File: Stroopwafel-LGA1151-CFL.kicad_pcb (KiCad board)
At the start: 2 copper layers, 4 parts

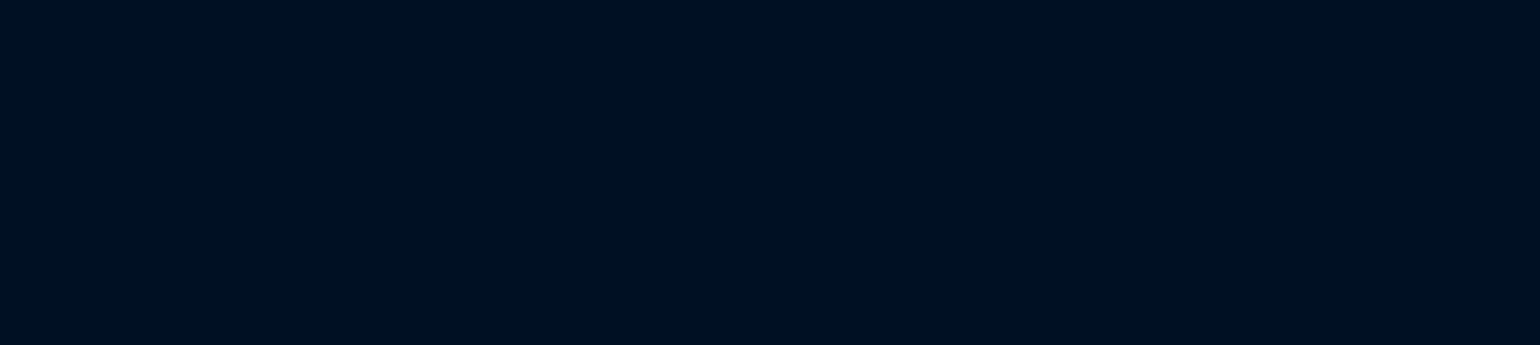
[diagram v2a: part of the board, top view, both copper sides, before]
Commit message: Added PCIe x16 slot
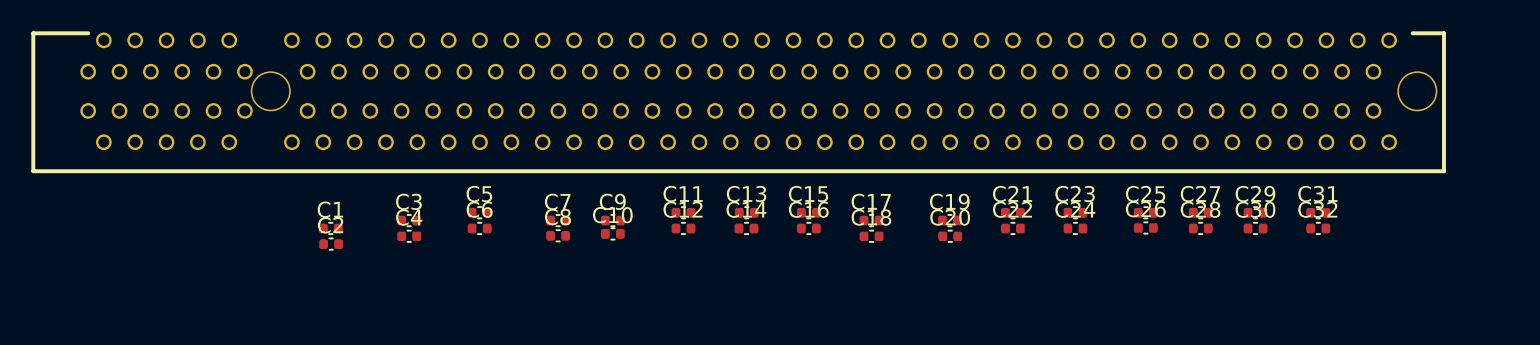
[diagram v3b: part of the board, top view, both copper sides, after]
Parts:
- added C1: 0.22uF, Capacitor_SMD:C_0402_1005Metric, F.Cu at (139.0, 38.0)
- added C10: 0.22uF, Capacitor_SMD:C_0402_1005Metric, F.Cu at (157.0, 38.4)
- added C11: 0.22uF, Capacitor_SMD:C_0402_1005Metric, F.Cu at (161.5, 37.0)
- added C12: 0.22uF, Capacitor_SMD:C_0402_1005Metric, F.Cu at (161.5, 38.0)
- added C13: 0.22uF, Capacitor_SMD:C_0402_1005Metric, F.Cu at (165.5, 37.0)
- added C14: 0.22uF, Capacitor_SMD:C_0402_1005Metric, F.Cu at (165.5, 38.0)
- added C15: 0.22uF, Capacitor_SMD:C_0402_1005Metric, F.Cu at (169.5, 37.0)
- added C16: 0.22uF, Capacitor_SMD:C_0402_1005Metric, F.Cu at (169.5, 38.0)
- added C17: 0.22uF, Capacitor_SMD:C_0402_1005Metric, F.Cu at (173.5, 37.5)
- added C18: 0.22uF, Capacitor_SMD:C_0402_1005Metric, F.Cu at (173.5, 38.5)
- added C19: 0.22uF, Capacitor_SMD:C_0402_1005Metric, F.Cu at (178.5, 37.5)
- added C2: 0.22uF, Capacitor_SMD:C_0402_1005Metric, F.Cu at (139.0, 39.0)
- added C20: 0.22uF, Capacitor_SMD:C_0402_1005Metric, F.Cu at (178.5, 38.5)
- added C21: 0.22uF, Capacitor_SMD:C_0402_1005Metric, F.Cu at (182.5, 37.0)
- added C22: 0.22uF, Capacitor_SMD:C_0402_1005Metric, F.Cu at (182.5, 38.0)
- added C23: 0.22uF, Capacitor_SMD:C_0402_1005Metric, F.Cu at (186.5, 37.0)
- added C24: 0.22uF, Capacitor_SMD:C_0402_1005Metric, F.Cu at (186.5, 38.0)
- added C25: 0.22uF, Capacitor_SMD:C_0402_1005Metric, F.Cu at (191.0, 37.0)
- added C26: 0.22uF, Capacitor_SMD:C_0402_1005Metric, F.Cu at (191.0, 38.0)
- added C27: 0.22uF, Capacitor_SMD:C_0402_1005Metric, F.Cu at (194.5, 37.0)
- added C28: 0.22uF, Capacitor_SMD:C_0402_1005Metric, F.Cu at (194.5, 38.0)
- added C29: 0.22uF, Capacitor_SMD:C_0402_1005Metric, F.Cu at (198.0, 37.0)
- added C3: 0.22uF, Capacitor_SMD:C_0402_1005Metric, F.Cu at (144.0, 37.5)
- added C30: 0.22uF, Capacitor_SMD:C_0402_1005Metric, F.Cu at (198.0, 38.0)
- added C31: 0.22uF, Capacitor_SMD:C_0402_1005Metric, F.Cu at (202.0, 37.0)
- added C32: 0.22uF, Capacitor_SMD:C_0402_1005Metric, F.Cu at (202.0, 38.0)
- added C4: 0.22uF, Capacitor_SMD:C_0402_1005Metric, F.Cu at (144.0, 38.5)
- added C5: 0.22uF, Capacitor_SMD:C_0402_1005Metric, F.Cu at (148.5, 37.0)
- added C6: 0.22uF, Capacitor_SMD:C_0402_1005Metric, F.Cu at (148.5, 38.0)
- added C7: 0.22uF, Capacitor_SMD:C_0402_1005Metric, F.Cu at (153.5, 37.5)
- added C8: 0.22uF, Capacitor_SMD:C_0402_1005Metric, F.Cu at (153.5, 38.5)
- added C9: 0.22uF, Capacitor_SMD:C_0402_1005Metric, F.Cu at (157.0, 37.5)
- added J1: PCIe_x16_full, A-my-stuff:PCIe_x16_tht_smallholes, F.Cu at (165.0, 29.2)
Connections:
- JCPU1 pad A5: unconnected-(JCPU1C-PEG_TXP_0-PadA5) -> PCIe_CPU_Tx0+
- JCPU1 pad A6: unconnected-(JCPU1C-PEG_TXN_0-PadA6) -> PCIe_CPU_Tx0-
- JCPU1 pad B4: unconnected-(JCPU1C-PEG_TXP_1-PadB4) -> PCIe_CPU_Tx1+
- JCPU1 pad B5: unconnected-(JCPU1C-PEG_TXN_1-PadB5) -> PCIe_CPU_Tx1-
- JCPU1 pad B7: unconnected-(JCPU1C-PEG_RXN_0-PadB7) -> PCIe_CPU_Rx0-
- JCPU1 pad B8: unconnected-(JCPU1C-PEG_RXP_0-PadB8) -> PCIe_CPU_Rx0+
- JCPU1 pad C3: unconnected-(JCPU1C-PEG_TXP_2-PadC3) -> PCIe_CPU_Tx2+
- JCPU1 pad C4: unconnected-(JCPU1C-PEG_TXN_2-PadC4) -> PCIe_CPU_Tx2-
- JCPU1 pad C6: unconnected-(JCPU1C-PEG_RXN_1-PadC6) -> PCIe_CPU_Rx1-
- JCPU1 pad C7: unconnected-(JCPU1C-PEG_RXP_1-PadC7) -> PCIe_CPU_Rx1+
- JCPU1 pad D2: unconnected-(JCPU1C-PEG_TXP_3-PadD2) -> PCIe_CPU_Tx3+
- JCPU1 pad D3: unconnected-(JCPU1C-PEG_TXN_3-PadD3) -> PCIe_CPU_Tx3-
- JCPU1 pad D5: unconnected-(JCPU1C-PEG_RXN_2-PadD5) -> PCIe_CPU_Rx2-
- JCPU1 pad D6: unconnected-(JCPU1C-PEG_RXP_2-PadD6) -> PCIe_CPU_Rx2+
- JCPU1 pad E1: unconnected-(JCPU1C-PEG_TXP_4-PadE1) -> PCIe_CPU_Tx4+
- JCPU1 pad E2: unconnected-(JCPU1C-PEG_TXN_4-PadE2) -> PCIe_CPU_Tx4-
- JCPU1 pad E4: unconnected-(JCPU1C-PEG_RXN_3-PadE4) -> PCIe_CPU_Rx3-
- JCPU1 pad E5: unconnected-(JCPU1C-PEG_RXP_3-PadE5) -> PCIe_CPU_Rx3+
- JCPU1 pad F2: unconnected-(JCPU1C-PEG_TXP_5-PadF2) -> PCIe_CPU_Tx5+
- JCPU1 pad F3: unconnected-(JCPU1C-PEG_TXN_5-PadF3) -> PCIe_CPU_Tx5-
- JCPU1 pad F5: unconnected-(JCPU1C-PEG_RXN_4-PadF5) -> PCIe_CPU_Rx4-
- JCPU1 pad F6: unconnected-(JCPU1C-PEG_RXP_4-PadF6) -> PCIe_CPU_Rx4+
- JCPU1 pad G1: unconnected-(JCPU1C-PEG_TXP_6-PadG1) -> PCIe_CPU_Tx6+
- JCPU1 pad G2: unconnected-(JCPU1C-PEG_TXN_6-PadG2) -> PCIe_CPU_Tx6-
- JCPU1 pad G4: unconnected-(JCPU1C-PEG_RXN_5-PadG4) -> PCIe_CPU_Rx5-
- JCPU1 pad G5: unconnected-(JCPU1C-PEG_RXP_5-PadG5) -> PCIe_CPU_Rx5+
- JCPU1 pad H2: unconnected-(JCPU1C-PEG_TXP_7-PadH2) -> PCIe_CPU_Tx7+
- JCPU1 pad H3: unconnected-(JCPU1C-PEG_TXN_7-PadH3) -> PCIe_CPU_Tx7-
- JCPU1 pad H5: unconnected-(JCPU1C-PEG_RXN_6-PadH5) -> PCIe_CPU_Rx6-
- JCPU1 pad H6: unconnected-(JCPU1C-PEG_RXP_6-PadH6) -> PCIe_CPU_Rx6+
- JCPU1 pad J1: unconnected-(JCPU1C-PEG_TXP_8-PadJ1) -> PCIe_CPU_Tx8+
- JCPU1 pad J2: unconnected-(JCPU1C-PEG_TXN_8-PadJ2) -> PCIe_CPU_Tx8-
- JCPU1 pad J4: unconnected-(JCPU1C-PEG_RXN_7-PadJ4) -> PCIe_CPU_Rx7-
- JCPU1 pad J5: unconnected-(JCPU1C-PEG_RXP_7-PadJ5) -> PCIe_CPU_Rx7+
- JCPU1 pad K2: unconnected-(JCPU1C-PEG_TXP_9-PadK2) -> PCIe_CPU_Tx9+
- JCPU1 pad K3: unconnected-(JCPU1C-PEG_TXN_9-PadK3) -> PCIe_CPU_Tx9-
- JCPU1 pad K5: unconnected-(JCPU1C-PEG_RXN_8-PadK5) -> PCIe_CPU_Rx8-
- JCPU1 pad K6: unconnected-(JCPU1C-PEG_RXP_8-PadK6) -> PCIe_CPU_Rx8+
- JCPU1 pad L1: unconnected-(JCPU1C-PEG_TXP_10-PadL1) -> PCIe_CPU_Tx10+
- JCPU1 pad L2: unconnected-(JCPU1C-PEG_TXN_10-PadL2) -> PCIe_CPU_Tx10-
- JCPU1 pad L4: unconnected-(JCPU1C-PEG_RXN_9-PadL4) -> PCIe_CPU_Rx9-
- JCPU1 pad L5: unconnected-(JCPU1C-PEG_RXP_9-PadL5) -> PCIe_CPU_Rx9+
- JCPU1 pad M2: unconnected-(JCPU1C-PEG_TXP_11-PadM2) -> PCIe_CPU_Tx11+
- JCPU1 pad M3: unconnected-(JCPU1C-PEG_TXN_11-PadM3) -> PCIe_CPU_Tx11-
- JCPU1 pad M5: unconnected-(JCPU1C-PEG_RXN_10-PadM5) -> PCIe_CPU_Rx10-
- JCPU1 pad M6: unconnected-(JCPU1C-PEG_RXP_10-PadM6) -> PCIe_CPU_Rx10+
- JCPU1 pad N1: unconnected-(JCPU1C-PEG_TXP_12-PadN1) -> PCIe_CPU_Tx12+
- JCPU1 pad N2: unconnected-(JCPU1C-PEG_TXN_12-PadN2) -> PCIe_CPU_Tx12-
- JCPU1 pad N4: unconnected-(JCPU1C-PEG_RXN_11-PadN4) -> PCIe_CPU_Rx11-
- JCPU1 pad N5: unconnected-(JCPU1C-PEG_RXP_11-PadN5) -> PCIe_CPU_Rx11+
- JCPU1 pad P2: unconnected-(JCPU1C-PEG_TXP_13-PadP2) -> PCIe_CPU_Tx13+
- JCPU1 pad P3: unconnected-(JCPU1C-PEG_TXN_13-PadP3) -> PCIe_CPU_Tx13-
- JCPU1 pad P5: unconnected-(JCPU1C-PEG_RXN_12-PadP5) -> PCIe_CPU_Rx12-
- JCPU1 pad P6: unconnected-(JCPU1C-PEG_RXP_12-PadP6) -> PCIe_CPU_Rx12+
- JCPU1 pad R1: unconnected-(JCPU1C-PEG_TXN_14-PadR1) -> PCIe_CPU_Tx14-
- JCPU1 pad R2: unconnected-(JCPU1C-PEG_TXP_14-PadR2) -> PCIe_CPU_Tx14+
- JCPU1 pad R4: unconnected-(JCPU1C-PEG_RXN_13-PadR4) -> PCIe_CPU_Rx13-
- JCPU1 pad R5: unconnected-(JCPU1C-PEG_RXP_13-PadR5) -> PCIe_CPU_Rx13+
- JCPU1 pad T2: unconnected-(JCPU1C-PEG_TXP_15-PadT2) -> PCIe_CPU_Tx15+
- JCPU1 pad T3: unconnected-(JCPU1C-PEG_TXN_15-PadT3) -> PCIe_CPU_Tx15-
- JCPU1 pad T5: unconnected-(JCPU1C-PEG_RXN_14-PadT5) -> PCIe_CPU_Rx14-
- JCPU1 pad T6: unconnected-(JCPU1C-PEG_RXP_14-PadT6) -> PCIe_CPU_Rx14+
- JCPU1 pad U4: unconnected-(JCPU1C-PEG_RXN_15-PadU4) -> PCIe_CPU_Rx15-
- JCPU1 pad U5: unconnected-(JCPU1C-PEG_RXP_15-PadU5) -> PCIe_CPU_Rx15+

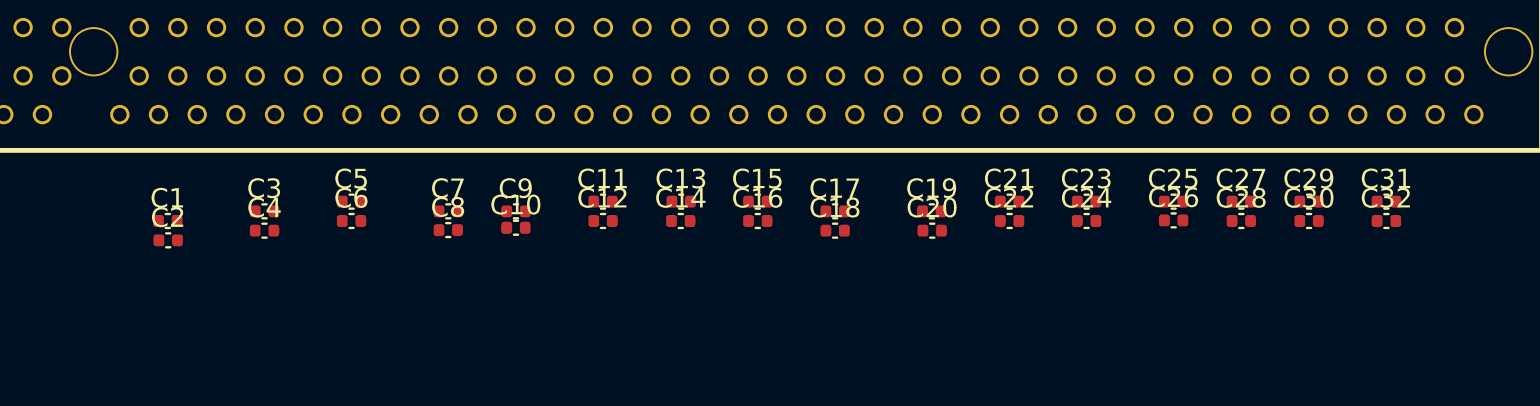
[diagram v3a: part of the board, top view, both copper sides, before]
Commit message: Added pcie slot and cpu clocks
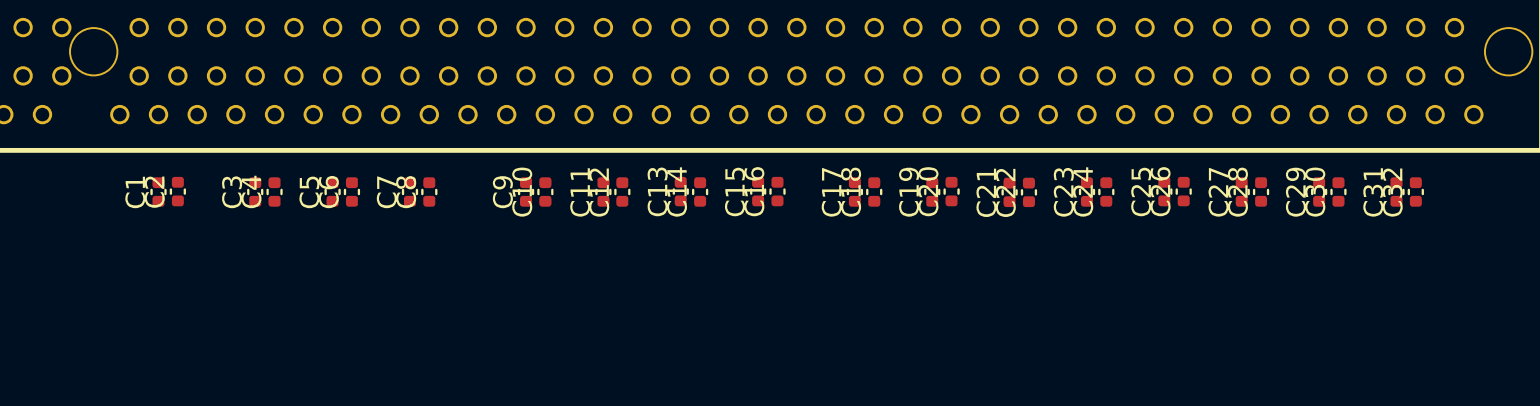
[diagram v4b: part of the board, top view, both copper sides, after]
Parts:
- J1: value PCIe_x16_full -> PCIe_x16_CPU
- moved C18 2.84 mm to (175.5, 36.5), turned to 90 degrees
- moved C2 2.57 mm to (139.5, 36.5), turned to 90 degrees
- moved C10 2.39 mm to (158.5, 36.5), turned to 90 degrees
- moved C20 2.25 mm to (179.5, 36.5), turned to 90 degrees
- moved C7 2.22 mm to (151.5, 36.5), turned to 90 degrees
- moved C8 2.20 mm to (152.5, 36.5), turned to 90 degrees
- moved C32 2.14 mm to (203.5, 36.5), turned to 90 degrees
- moved C30 2.14 mm to (199.5, 36.5), turned to 90 degrees
- moved C4 2.07 mm to (144.5, 36.5), turned to 90 degrees
- moved C16 1.83 mm to (170.5, 36.5), turned to 90 degrees
- moved C24 1.81 mm to (187.5, 36.5), turned to 90 degrees
- moved C28 1.81 mm to (195.5, 36.5), turned to 90 degrees
- moved C12 1.80 mm to (162.5, 36.5), turned to 90 degrees
- moved C14 1.80 mm to (166.5, 36.5), turned to 90 degrees
- moved C22 1.79 mm to (183.5, 36.5), turned to 90 degrees
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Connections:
- net /CPU_PEG_DMI/PCIe_CPU_C_Tx0+ renamed /PCIe_slots/PCIe_CPU_C_Tx0+
- net /CPU_PEG_DMI/PCIe_CPU_C_Tx0- renamed /PCIe_slots/PCIe_CPU_C_Tx0-
- net /CPU_PEG_DMI/PCIe_CPU_C_Tx1+ renamed /PCIe_slots/PCIe_CPU_C_Tx1+
- net /CPU_PEG_DMI/PCIe_CPU_C_Tx1- renamed /PCIe_slots/PCIe_CPU_C_Tx1-
- net /CPU_PEG_DMI/PCIe_CPU_C_Tx10+ renamed /PCIe_slots/PCIe_CPU_C_Tx10+
- net /CPU_PEG_DMI/PCIe_CPU_C_Tx10- renamed /PCIe_slots/PCIe_CPU_C_Tx10-
- net /CPU_PEG_DMI/PCIe_CPU_C_Tx11+ renamed /PCIe_slots/PCIe_CPU_C_Tx11+
- net /CPU_PEG_DMI/PCIe_CPU_C_Tx11- renamed /PCIe_slots/PCIe_CPU_C_Tx11-
- net /CPU_PEG_DMI/PCIe_CPU_C_Tx12+ renamed /PCIe_slots/PCIe_CPU_C_Tx12+
- net /CPU_PEG_DMI/PCIe_CPU_C_Tx12- renamed /PCIe_slots/PCIe_CPU_C_Tx12-
- net /CPU_PEG_DMI/PCIe_CPU_C_Tx13+ renamed /PCIe_slots/PCIe_CPU_C_Tx13+
- net /CPU_PEG_DMI/PCIe_CPU_C_Tx13- renamed /PCIe_slots/PCIe_CPU_C_Tx13-
- net /CPU_PEG_DMI/PCIe_CPU_C_Tx14+ renamed /PCIe_slots/PCIe_CPU_C_Tx14+
- net /CPU_PEG_DMI/PCIe_CPU_C_Tx14- renamed /PCIe_slots/PCIe_CPU_C_Tx14-
- net /CPU_PEG_DMI/PCIe_CPU_C_Tx15+ renamed /PCIe_slots/PCIe_CPU_C_Tx15+
- net /CPU_PEG_DMI/PCIe_CPU_C_Tx15- renamed /PCIe_slots/PCIe_CPU_C_Tx15-
- net /CPU_PEG_DMI/PCIe_CPU_C_Tx2+ renamed /PCIe_slots/PCIe_CPU_C_Tx2+
- net /CPU_PEG_DMI/PCIe_CPU_C_Tx2- renamed /PCIe_slots/PCIe_CPU_C_Tx2-
- net /CPU_PEG_DMI/PCIe_CPU_C_Tx3+ renamed /PCIe_slots/PCIe_CPU_C_Tx3+
- net /CPU_PEG_DMI/PCIe_CPU_C_Tx3- renamed /PCIe_slots/PCIe_CPU_C_Tx3-
- net /CPU_PEG_DMI/PCIe_CPU_C_Tx4+ renamed /PCIe_slots/PCIe_CPU_C_Tx4+
- net /CPU_PEG_DMI/PCIe_CPU_C_Tx4- renamed /PCIe_slots/PCIe_CPU_C_Tx4-
- net /CPU_PEG_DMI/PCIe_CPU_C_Tx5+ renamed /PCIe_slots/PCIe_CPU_C_Tx5+
- net /CPU_PEG_DMI/PCIe_CPU_C_Tx5- renamed /PCIe_slots/PCIe_CPU_C_Tx5-
- net /CPU_PEG_DMI/PCIe_CPU_C_Tx6+ renamed /PCIe_slots/PCIe_CPU_C_Tx6+
- net /CPU_PEG_DMI/PCIe_CPU_C_Tx6- renamed /PCIe_slots/PCIe_CPU_C_Tx6-
- net /CPU_PEG_DMI/PCIe_CPU_C_Tx7+ renamed /PCIe_slots/PCIe_CPU_C_Tx7+
- net /CPU_PEG_DMI/PCIe_CPU_C_Tx7- renamed /PCIe_slots/PCIe_CPU_C_Tx7-
- net /CPU_PEG_DMI/PCIe_CPU_C_Tx8+ renamed /PCIe_slots/PCIe_CPU_C_Tx8+
- net /CPU_PEG_DMI/PCIe_CPU_C_Tx8- renamed /PCIe_slots/PCIe_CPU_C_Tx8-
- net /CPU_PEG_DMI/PCIe_CPU_C_Tx9+ renamed /PCIe_slots/PCIe_CPU_C_Tx9+
- net /CPU_PEG_DMI/PCIe_CPU_C_Tx9- renamed /PCIe_slots/PCIe_CPU_C_Tx9-
- J1 pad A1: unconnected-(J1-~{PRSNT1}-PadA1) -> GND
- J1 pad A13: unconnected-(J1-REFCLK+-PadA13) -> PCIe_CPU_Refclk+
- J1 pad A14: unconnected-(J1-REFCLK--PadA14) -> PCIe_CPU_Refclk-
- J1 pad B17: unconnected-(J1-~{PRSNT2}-PadB17) -> PCIe_CPU_CLKREQ#
- J1 pad B31: unconnected-(J1-~{PRSNT2}-PadB31) -> PCIe_CPU_CLKREQ#
- J1 pad B48: unconnected-(J1-~{PRSNT2}-PadB48) -> PCIe_CPU_CLKREQ#
- J1 pad B81: unconnected-(J1-~{PRSNT2}-PadB81) -> PCIe_CPU_CLKREQ#
- JCPU1 pad J9: unconnected-(JCPU1E-CLK24N-PadJ9) -> CPU_24MCLK-
- JCPU1 pad K9: unconnected-(JCPU1E-CLK24P-PadK9) -> CPU_24MCLK+
- JCPU1 pad W1: unconnected-(JCPU1E-PCI_BCLKP-PadW1) -> CPU_PCIBCLK+
- JCPU1 pad W2: unconnected-(JCPU1E-PCI_BCLKN-PadW2) -> CPU_PCIBCLK-
- JCPU1 pad W4: unconnected-(JCPU1E-BCLKN-PadW4) -> CPU_BCLK-
- JCPU1 pad W5: unconnected-(JCPU1E-BCLKP-PadW5) -> CPU_BCLK+
- UPCH1 pad A6: unconnected-(UPCH1G-CLKOUT_CPUPCIBCLK_P-PadA6) -> CPU_PCIBCLK+
- UPCH1 pad AJ6: unconnected-(UPCH1G-CLKOUT_PCIE_N0-PadAJ6) -> PCIe_CPU_Refclk-
- UPCH1 pad AJ7: unconnected-(UPCH1G-CLKOUT_PCIE_P0-PadAJ7) -> PCIe_CPU_Refclk+
- UPCH1 pad B6: unconnected-(UPCH1G-CLKOUT_CPUPCIBCLK_N-PadB6) -> CPU_PCIBCLK-
- UPCH1 pad B8: unconnected-(UPCH1G-CLKOUT_CPUBCLK_P-PadB8) -> CPU_BCLK+
- UPCH1 pad BF31: unconnected-(UPCH1G-GPP_B5/SRCCLKREQ0#-PadBF31) -> PCIe_CPU_CLKREQ#
- UPCH1 pad C6: unconnected-(UPCH1G-CLKOUT_CPUNSSC_N-PadC6) -> CPU_24MCLK-
- UPCH1 pad C8: unconnected-(UPCH1G-CLKOUT_CPUBCLK_N-PadC8) -> CPU_BCLK-
- UPCH1 pad D7: unconnected-(UPCH1G-CLKOUT_CPUNSSC_P-PadD7) -> CPU_24MCLK+

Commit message: Some DP and power work
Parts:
- added C33: 0.1uF, Capacitor_SMD:C_0402_1005Metric, F.Cu at (226.4, 40.5)
- added C34: 0.1uF, Capacitor_SMD:C_0402_1005Metric, F.Cu at (228.4, 40.5)
- added C35: 0.1uF, Capacitor_SMD:C_0402_1005Metric, F.Cu at (230.3, 40.5)
- added C36: 0.1uF, Capacitor_SMD:C_0402_1005Metric, F.Cu at (232.3, 40.5)
- added C37: 0.1uF, Capacitor_SMD:C_0402_1005Metric, F.Cu at (234.3, 40.5)
- added C38: 0.1uF, Capacitor_SMD:C_0402_1005Metric, F.Cu at (236.3, 40.5)
- added C39: 0.1uF, Capacitor_SMD:C_0402_1005Metric, F.Cu at (238.2, 40.5)
- added C40: 0.1uF, Capacitor_SMD:C_0402_1005Metric, F.Cu at (240.2, 40.5)
- added J2: DP_A, A-my-stuff:DP-SMD_HYC16-DP20-178, F.Cu at (233.5, 31.4)
- added R1: 30Ω, Resistor_SMD:R_0402_1005Metric, F.Cu at (161.4, 45.6)
- added R2: 20Ω, Resistor_SMD:R_0402_1005Metric, F.Cu at (161.4, 47.6)
- added R3: 30Ω, Resistor_SMD:R_0402_1005Metric, F.Cu at (161.4, 49.6)
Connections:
- JCPU1 pad A23: unconnected-(JCPU1D-DDI1_TXN_2-PadA23) -> iGPU_DDI1_TX2-
- JCPU1 pad A25: unconnected-(JCPU1G-VCC_CORE-PadA25) -> VCC_CORE
- JCPU1 pad A26: unconnected-(JCPU1G-VCC_CORE-PadA26) -> VCC_CORE
- JCPU1 pad A27: unconnected-(JCPU1G-VCC_CORE-PadA27) -> VCC_CORE
- JCPU1 pad A28: unconnected-(JCPU1G-VCC_CORE-PadA28) -> VCC_CORE
- JCPU1 pad A29: unconnected-(JCPU1G-VCC_CORE-PadA29) -> VCC_CORE
- JCPU1 pad A30: unconnected-(JCPU1G-VCC_CORE-PadA30) -> VCC_CORE
- JCPU1 pad AA34: unconnected-(JCPU1H-VCCGT-PadAA34) -> VCC_iGPU
- JCPU1 pad AA35: unconnected-(JCPU1H-VCCGT-PadAA35) -> VCC_iGPU
- JCPU1 pad AA36: unconnected-(JCPU1H-VCCGT-PadAA36) -> VCC_iGPU
- JCPU1 pad AA37: unconnected-(JCPU1H-VCCGT-PadAA37) -> VCC_iGPU
- JCPU1 pad AA38: unconnected-(JCPU1H-VCCGT-PadAA38) -> VCC_iGPU
- JCPU1 pad AA6: unconnected-(JCPU1I-VCCSA-PadAA6) -> VCCSA
- JCPU1 pad AA7: unconnected-(JCPU1I-VCCSA-PadAA7) -> VCCSA
- JCPU1 pad AB33: unconnected-(JCPU1H-VCCGT-PadAB33) -> VCC_iGPU
- JCPU1 pad AB34: unconnected-(JCPU1H-VCCGT-PadAB34) -> VCC_iGPU
- JCPU1 pad AB6: unconnected-(JCPU1I-VCCSA-PadAB6) -> VCCSA
- JCPU1 pad AB7: unconnected-(JCPU1I-VCCSA-PadAB7) -> VCCSA
- JCPU1 pad AB8: unconnected-(JCPU1I-VCCSA-PadAB8) -> VCCSA
- JCPU1 pad AC7: unconnected-(JCPU1I-VCCSA-PadAC7) -> VCCSA
- JCPU1 pad AC8: unconnected-(JCPU1I-VCCSA-PadAC8) -> VCCSA
- JCPU1 pad AJ11: unconnected-(JCPU1G-VCC_CORE-PadAJ11) -> VCC_CORE
- JCPU1 pad AJ12: unconnected-(JCPU1G-VCC_CORE-PadAJ12) -> VCC_CORE
- JCPU1 pad AJ13: unconnected-(JCPU1G-VCC_CORE-PadAJ13) -> VCC_CORE
- JCPU1 pad AJ14: unconnected-(JCPU1G-VCC_CORE-PadAJ14) -> VCC_CORE
- JCPU1 pad AJ15: unconnected-(JCPU1G-VCC_CORE-PadAJ15) -> VCC_CORE
- JCPU1 pad AJ16: unconnected-(JCPU1G-VCC_CORE-PadAJ16) -> VCC_CORE
- JCPU1 pad AJ17: unconnected-(JCPU1G-VCC_CORE-PadAJ17) -> VCC_CORE
- JCPU1 pad AJ18: unconnected-(JCPU1G-VCC_CORE-PadAJ18) -> VCC_CORE
- JCPU1 pad AJ19: unconnected-(JCPU1G-VCC_CORE-PadAJ19) -> VCC_CORE
- JCPU1 pad AJ20: unconnected-(JCPU1G-VCC_CORE-PadAJ20) -> VCC_CORE
- JCPU1 pad AJ21: unconnected-(JCPU1G-VCC_CORE-PadAJ21) -> VCC_CORE
- JCPU1 pad AJ23: unconnected-(JCPU1I-VCCIO-PadAJ23) -> VCCIO
- JCPU1 pad AJ25: unconnected-(JCPU1G-VCC_CORE-PadAJ25) -> VCC_CORE
- JCPU1 pad AJ26: unconnected-(JCPU1G-VCC_CORE-PadAJ26) -> VCC_CORE
- JCPU1 pad AJ27: unconnected-(JCPU1G-VCC_CORE-PadAJ27) -> VCC_CORE
- JCPU1 pad AJ28: unconnected-(JCPU1G-VCC_CORE-PadAJ28) -> VCC_CORE
- JCPU1 pad AJ29: unconnected-(JCPU1G-VCC_CORE-PadAJ29) -> VCC_CORE
- JCPU1 pad AK11: unconnected-(JCPU1I-VCCIO-PadAK11) -> VCCIO
- JCPU1 pad AK14: unconnected-(JCPU1I-VCCIO-PadAK14) -> VCCIO
- JCPU1 pad AK21: unconnected-(JCPU1G-VCC_CORE-PadAK21) -> VCC_CORE
- JCPU1 pad AK24: unconnected-(JCPU1I-VCCIO-PadAK24) -> VCCIO
- JCPU1 pad AT18: unconnected-(JCPU1I-VDDQ-PadAT18) -> VDDQ
- JCPU1 pad AT21: unconnected-(JCPU1I-VDDQ-PadAT21) -> VDDQ
- JCPU1 pad AU13: unconnected-(JCPU1I-VDDQ-PadAU13) -> VDDQ
- JCPU1 pad AU15: unconnected-(JCPU1I-VDDQ-PadAU15) -> VDDQ
- JCPU1 pad AU19: unconnected-(JCPU1I-VDDQ-PadAU19) -> VDDQ
- JCPU1 pad AU23: unconnected-(JCPU1I-VDDQ-PadAU23) -> VDDQ
- JCPU1 pad AV11: unconnected-(JCPU1I-VDDQ-PadAV11) -> VDDQ
- JCPU1 pad AV17: unconnected-(JCPU1I-VDDQ-PadAV17) -> VDDQ
- JCPU1 pad AV21: unconnected-(JCPU1I-VDDQ-PadAV21) -> VDDQ
- JCPU1 pad AW10: unconnected-(JCPU1I-VDDQ-PadAW10) -> VDDQ
- JCPU1 pad AW14: unconnected-(JCPU1I-VDDQ-PadAW14) -> VDDQ
- JCPU1 pad AW25: unconnected-(JCPU1I-VDDQ-PadAW25) -> VDDQ
- JCPU1 pad AY12: unconnected-(JCPU1I-VDDQ-PadAY12) -> VDDQ
- JCPU1 pad AY16: unconnected-(JCPU1I-VDDQ-PadAY16) -> VDDQ
- JCPU1 pad AY18: unconnected-(JCPU1I-VDDQ-PadAY18) -> VDDQ
- JCPU1 pad AY23: unconnected-(JCPU1I-VDDQ-PadAY23) -> VDDQ
- JCPU1 pad B13: unconnected-(JCPU1D-DDI1_AUXP-PadB13) -> iGPU_DDI1_AUX+
- JCPU1 pad B23: unconnected-(JCPU1D-DDI1_TXP_2-PadB23) -> iGPU_DDI1_TX2+
- JCPU1 pad B25: unconnected-(JCPU1G-VCC_CORE-PadB25) -> VCC_CORE
- JCPU1 pad B27: unconnected-(JCPU1G-VCC_CORE-PadB27) -> VCC_CORE
- JCPU1 pad B29: unconnected-(JCPU1G-VCC_CORE-PadB29) -> VCC_CORE
- JCPU1 pad B31: unconnected-(JCPU1G-VCC_CORE-PadB31) -> VCC_CORE
- JCPU1 pad B32: unconnected-(JCPU1G-VCC_CORE-PadB32) -> VCC_CORE
- JCPU1 pad B33: unconnected-(JCPU1G-VCC_CORE-PadB33) -> VCC_CORE
- JCPU1 pad B34: unconnected-(JCPU1G-VCC_CORE-PadB34) -> VCC_CORE
- JCPU1 pad B35: unconnected-(JCPU1G-VCC_CORE-PadB35) -> VCC_CORE
- JCPU1 pad B36: unconnected-(JCPU1G-VCC_CORE-PadB36) -> VCC_CORE
- JCPU1 pad B37: unconnected-(JCPU1G-VCC_CORE-PadB37) -> VCC_CORE
- JCPU1 pad C13: unconnected-(JCPU1D-DDI1_AUXN-PadC13) -> iGPU_DDI1_AUX-
- JCPU1 pad C21: unconnected-(JCPU1D-DDI1_TXP_0-PadC21) -> iGPU_DDI1_TX0+
- JCPU1 pad C23: unconnected-(JCPU1D-DDI1_TXP_3-PadC23) -> iGPU_DDI1_TX3+
- JCPU1 pad C25: unconnected-(JCPU1G-VCC_CORE-PadC25) -> VCC_CORE
- JCPU1 pad C26: unconnected-(JCPU1G-VCC_CORE-PadC26) -> VCC_CORE
- JCPU1 pad C27: unconnected-(JCPU1G-VCC_CORE-PadC27) -> VCC_CORE
- JCPU1 pad C28: unconnected-(JCPU1G-VCC_CORE-PadC28) -> VCC_CORE
- JCPU1 pad C29: unconnected-(JCPU1G-VCC_CORE-PadC29) -> VCC_CORE
- JCPU1 pad C30: unconnected-(JCPU1G-VCC_CORE-PadC30) -> VCC_CORE
- JCPU1 pad C32: unconnected-(JCPU1G-VCC_CORE-PadC32) -> VCC_CORE
- JCPU1 pad C34: unconnected-(JCPU1G-VCC_CORE-PadC34) -> VCC_CORE
- JCPU1 pad C36: unconnected-(JCPU1G-VCC_CORE-PadC36) -> VCC_CORE
- JCPU1 pad D21: unconnected-(JCPU1D-DDI1_TXN_0-PadD21) -> iGPU_DDI1_TX0-
- JCPU1 pad D22: unconnected-(JCPU1D-DDI1_TXP_1-PadD22) -> iGPU_DDI1_TX1+
- JCPU1 pad D23: unconnected-(JCPU1D-DDI1_TXN_3-PadD23) -> iGPU_DDI1_TX3-
- JCPU1 pad D25: unconnected-(JCPU1G-VCC_CORE-PadD25) -> VCC_CORE
- JCPU1 pad D27: unconnected-(JCPU1G-VCC_CORE-PadD27) -> VCC_CORE
- JCPU1 pad D29: unconnected-(JCPU1G-VCC_CORE-PadD29) -> VCC_CORE
- JCPU1 pad D31: unconnected-(JCPU1G-VCC_CORE-PadD31) -> VCC_CORE
- JCPU1 pad D32: unconnected-(JCPU1G-VCC_CORE-PadD32) -> VCC_CORE
- JCPU1 pad D33: unconnected-(JCPU1G-VCC_CORE-PadD33) -> VCC_CORE
- JCPU1 pad D34: unconnected-(JCPU1G-VCC_CORE-PadD34) -> VCC_CORE
- JCPU1 pad D35: unconnected-(JCPU1G-VCC_CORE-PadD35) -> VCC_CORE
- JCPU1 pad D36: unconnected-(JCPU1G-VCC_CORE-PadD36) -> VCC_CORE
- JCPU1 pad E22: unconnected-(JCPU1D-DDI1_TXN_1-PadE22) -> iGPU_DDI1_TX1-
- JCPU1 pad E24: unconnected-(JCPU1G-VCC_CORE-PadE24) -> VCC_CORE
- JCPU1 pad E25: unconnected-(JCPU1G-VCC_CORE-PadE25) -> VCC_CORE
- JCPU1 pad E26: unconnected-(JCPU1G-VCC_CORE-PadE26) -> VCC_CORE
- JCPU1 pad E27: unconnected-(JCPU1G-VCC_CORE-PadE27) -> VCC_CORE
- JCPU1 pad E28: unconnected-(JCPU1G-VCC_CORE-PadE28) -> VCC_CORE
- JCPU1 pad E29: unconnected-(JCPU1G-VCC_CORE-PadE29) -> VCC_CORE
- JCPU1 pad E30: unconnected-(JCPU1G-VCC_CORE-PadE30) -> VCC_CORE
- JCPU1 pad E32: unconnected-(JCPU1G-VCC_CORE-PadE32) -> VCC_CORE
- JCPU1 pad E34: unconnected-(JCPU1G-VCC_CORE-PadE34) -> VCC_CORE
- JCPU1 pad E36: unconnected-(JCPU1G-VCC_CORE-PadE36) -> VCC_CORE
- JCPU1 pad F23: unconnected-(JCPU1G-VCC_CORE-PadF23) -> VCC_CORE
- JCPU1 pad F24: unconnected-(JCPU1G-VCC_CORE-PadF24) -> VCC_CORE
- JCPU1 pad F25: unconnected-(JCPU1G-VCC_CORE-PadF25) -> VCC_CORE
- JCPU1 pad F27: unconnected-(JCPU1G-VCC_CORE-PadF27) -> VCC_CORE
- JCPU1 pad F29: unconnected-(JCPU1G-VCC_CORE-PadF29) -> VCC_CORE
- JCPU1 pad F31: unconnected-(JCPU1G-VCC_CORE-PadF31) -> VCC_CORE
- JCPU1 pad F32: unconnected-(JCPU1G-VCC_CORE-PadF32) -> VCC_CORE
- JCPU1 pad F33: unconnected-(JCPU1G-VCC_CORE-PadF33) -> VCC_CORE
- JCPU1 pad F34: unconnected-(JCPU1G-VCC_CORE-PadF34) -> VCC_CORE
- JCPU1 pad F35: unconnected-(JCPU1G-VCC_CORE-PadF35) -> VCC_CORE
- JCPU1 pad F37: unconnected-(JCPU1G-VCC_CORE-PadF37) -> VCC_CORE
- JCPU1 pad G23: unconnected-(JCPU1G-VCC_CORE-PadG23) -> VCC_CORE
- JCPU1 pad G24: unconnected-(JCPU1G-VCC_CORE-PadG24) -> VCC_CORE
- JCPU1 pad G25: unconnected-(JCPU1G-VCC_CORE-PadG25) -> VCC_CORE
- JCPU1 pad G26: unconnected-(JCPU1G-VCC_CORE-PadG26) -> VCC_CORE
- JCPU1 pad G27: unconnected-(JCPU1G-VCC_CORE-PadG27) -> VCC_CORE
- JCPU1 pad G28: unconnected-(JCPU1G-VCC_CORE-PadG28) -> VCC_CORE
- JCPU1 pad G29: unconnected-(JCPU1G-VCC_CORE-PadG29) -> VCC_CORE
- JCPU1 pad G30: unconnected-(JCPU1G-VCC_CORE-PadG30) -> VCC_CORE
- JCPU1 pad G32: unconnected-(JCPU1G-VCC_CORE-PadG32) -> VCC_CORE
- JCPU1 pad G34: unconnected-(JCPU1G-VCC_CORE-PadG34) -> VCC_CORE
- JCPU1 pad G35: unconnected-(JCPU1G-VCC_CORE-PadG35) -> VCC_CORE
- JCPU1 pad G36: unconnected-(JCPU1H-VCCGT-PadG36) -> VCC_iGPU
- JCPU1 pad G37: unconnected-(JCPU1H-VCCGT-PadG37) -> VCC_iGPU
- JCPU1 pad G38: unconnected-(JCPU1H-VCCGT-PadG38) -> VCC_iGPU
- JCPU1 pad G39: unconnected-(JCPU1H-VCCGT-PadG39) -> VCC_iGPU
- JCPU1 pad G40: unconnected-(JCPU1H-VCCGT-PadG40) -> VCC_iGPU
- JCPU1 pad H22: unconnected-(JCPU1G-VCC_CORE-PadH22) -> VCC_CORE
- JCPU1 pad H23: unconnected-(JCPU1G-VCC_CORE-PadH23) -> VCC_CORE
- JCPU1 pad H25: unconnected-(JCPU1G-VCC_CORE-PadH25) -> VCC_CORE
- JCPU1 pad H27: unconnected-(JCPU1G-VCC_CORE-PadH27) -> VCC_CORE
- JCPU1 pad H29: unconnected-(JCPU1G-VCC_CORE-PadH29) -> VCC_CORE
- JCPU1 pad H31: unconnected-(JCPU1G-VCC_CORE-PadH31) -> VCC_CORE
- JCPU1 pad H32: unconnected-(JCPU1G-VCC_CORE-PadH32) -> VCC_CORE
- JCPU1 pad H33: unconnected-(JCPU1G-VCC_CORE-PadH33) -> VCC_CORE
- JCPU1 pad H34: unconnected-(JCPU1G-VCC_CORE-PadH34) -> VCC_CORE
- JCPU1 pad H36: unconnected-(JCPU1H-VCCGT-PadH36) -> VCC_iGPU
- JCPU1 pad H38: unconnected-(JCPU1H-VCCGT-PadH38) -> VCC_iGPU
- JCPU1 pad H40: unconnected-(JCPU1H-VCCGT-PadH40) -> VCC_iGPU
- JCPU1 pad J21: unconnected-(JCPU1G-VCC_CORE-PadJ21) -> VCC_CORE
- JCPU1 pad J22: unconnected-(JCPU1G-VCC_CORE-PadJ22) -> VCC_CORE
- JCPU1 pad J23: unconnected-(JCPU1G-VCC_CORE-PadJ23) -> VCC_CORE
- JCPU1 pad J24: unconnected-(JCPU1G-VCC_CORE-PadJ24) -> VCC_CORE
- JCPU1 pad J25: unconnected-(JCPU1G-VCC_CORE-PadJ25) -> VCC_CORE
- JCPU1 pad J26: unconnected-(JCPU1G-VCC_CORE-PadJ26) -> VCC_CORE
- JCPU1 pad J27: unconnected-(JCPU1G-VCC_CORE-PadJ27) -> VCC_CORE
- JCPU1 pad J28: unconnected-(JCPU1G-VCC_CORE-PadJ28) -> VCC_CORE
- JCPU1 pad J29: unconnected-(JCPU1G-VCC_CORE-PadJ29) -> VCC_CORE
- JCPU1 pad J30: unconnected-(JCPU1G-VCC_CORE-PadJ30) -> VCC_CORE
- JCPU1 pad J31: unconnected-(JCPU1G-VCC_CORE-PadJ31) -> VCC_CORE
- JCPU1 pad J33: unconnected-(JCPU1G-VCC_CORE-PadJ33) -> VCC_CORE
- JCPU1 pad J35: unconnected-(JCPU1G-VCC_CORE-PadJ35) -> VCC_CORE
- JCPU1 pad J36: unconnected-(JCPU1H-VCCGT-PadJ36) -> VCC_iGPU
- JCPU1 pad J37: unconnected-(JCPU1H-VCCGT-PadJ37) -> VCC_iGPU
- JCPU1 pad J38: unconnected-(JCPU1H-VCCGT-PadJ38) -> VCC_iGPU
- JCPU1 pad J39: unconnected-(JCPU1H-VCCGT-PadJ39) -> VCC_iGPU
- JCPU1 pad J40: unconnected-(JCPU1H-VCCGT-PadJ40) -> VCC_iGPU
- JCPU1 pad K16: unconnected-(JCPU1G-VCC_CORE-PadK16) -> VCC_CORE
- JCPU1 pad K18: unconnected-(JCPU1G-VCC_CORE-PadK18) -> VCC_CORE
- JCPU1 pad K20: unconnected-(JCPU1G-VCC_CORE-PadK20) -> VCC_CORE
- JCPU1 pad K21: unconnected-(JCPU1G-VCC_CORE-PadK21) -> VCC_CORE
- JCPU1 pad K23: unconnected-(JCPU1G-VCC_CORE-PadK23) -> VCC_CORE
- JCPU1 pad K25: unconnected-(JCPU1G-VCC_CORE-PadK25) -> VCC_CORE
- JCPU1 pad K27: unconnected-(JCPU1G-VCC_CORE-PadK27) -> VCC_CORE
- JCPU1 pad K29: unconnected-(JCPU1G-VCC_CORE-PadK29) -> VCC_CORE
- JCPU1 pad K31: unconnected-(JCPU1G-VCC_CORE-PadK31) -> VCC_CORE
- JCPU1 pad K32: unconnected-(JCPU1G-VCC_CORE-PadK32) -> VCC_CORE
- JCPU1 pad K34: unconnected-(JCPU1G-VCC_CORE-PadK34) -> VCC_CORE
- JCPU1 pad K36: unconnected-(JCPU1H-VCCGT-PadK36) -> VCC_iGPU
- JCPU1 pad K38: unconnected-(JCPU1H-VCCGT-PadK38) -> VCC_iGPU
- JCPU1 pad K40: unconnected-(JCPU1H-VCCGT-PadK40) -> VCC_iGPU
- JCPU1 pad L14: unconnected-(JCPU1G-VCC_CORE-PadL14) -> VCC_CORE
- JCPU1 pad L15: unconnected-(JCPU1G-VCC_CORE-PadL15) -> VCC_CORE
- JCPU1 pad L16: unconnected-(JCPU1G-VCC_CORE-PadL16) -> VCC_CORE
- JCPU1 pad L17: unconnected-(JCPU1G-VCC_CORE-PadL17) -> VCC_CORE
- JCPU1 pad L18: unconnected-(JCPU1G-VCC_CORE-PadL18) -> VCC_CORE
- JCPU1 pad L19: unconnected-(JCPU1G-VCC_CORE-PadL19) -> VCC_CORE
- JCPU1 pad L20: unconnected-(JCPU1G-VCC_CORE-PadL20) -> VCC_CORE
- JCPU1 pad L21: unconnected-(JCPU1G-VCC_CORE-PadL21) -> VCC_CORE
- JCPU1 pad L22: unconnected-(JCPU1G-VCC_CORE-PadL22) -> VCC_CORE
- JCPU1 pad L23: unconnected-(JCPU1G-VCC_CORE-PadL23) -> VCC_CORE
- JCPU1 pad L24: unconnected-(JCPU1G-VCC_CORE-PadL24) -> VCC_CORE
- JCPU1 pad L25: unconnected-(JCPU1G-VCC_CORE-PadL25) -> VCC_CORE
- JCPU1 pad L26: unconnected-(JCPU1G-VCC_CORE-PadL26) -> VCC_CORE
- JCPU1 pad L27: unconnected-(JCPU1G-VCC_CORE-PadL27) -> VCC_CORE
- JCPU1 pad L28: unconnected-(JCPU1G-VCC_CORE-PadL28) -> VCC_CORE
- JCPU1 pad L29: unconnected-(JCPU1G-VCC_CORE-PadL29) -> VCC_CORE
- JCPU1 pad L30: unconnected-(JCPU1G-VCC_CORE-PadL30) -> VCC_CORE
- JCPU1 pad L31: unconnected-(JCPU1G-VCC_CORE-PadL31) -> VCC_CORE
- JCPU1 pad L33: unconnected-(JCPU1G-VCC_CORE-PadL33) -> VCC_CORE
- JCPU1 pad L34: unconnected-(JCPU1H-VCCGT-PadL34) -> VCC_iGPU
- JCPU1 pad L35: unconnected-(JCPU1H-VCCGT-PadL35) -> VCC_iGPU
- JCPU1 pad L36: unconnected-(JCPU1H-VCCGT-PadL36) -> VCC_iGPU
- JCPU1 pad L37: unconnected-(JCPU1H-VCCGT-PadL37) -> VCC_iGPU
- JCPU1 pad L38: unconnected-(JCPU1H-VCCGT-PadL38) -> VCC_iGPU
- JCPU1 pad L39: unconnected-(JCPU1H-VCCGT-PadL39) -> VCC_iGPU
- JCPU1 pad L40: unconnected-(JCPU1H-VCCGT-PadL40) -> VCC_iGPU
- JCPU1 pad M13: unconnected-(JCPU1G-VCC_CORE-PadM13) -> VCC_CORE
- JCPU1 pad M14: unconnected-(JCPU1G-VCC_CORE-PadM14) -> VCC_CORE
- JCPU1 pad M16: unconnected-(JCPU1G-VCC_CORE-PadM16) -> VCC_CORE
- JCPU1 pad M18: unconnected-(JCPU1G-VCC_CORE-PadM18) -> VCC_CORE
- JCPU1 pad M20: unconnected-(JCPU1G-VCC_CORE-PadM20) -> VCC_CORE
- JCPU1 pad M22: unconnected-(JCPU1G-VCC_CORE-PadM22) -> VCC_CORE
- JCPU1 pad M24: unconnected-(JCPU1G-VCC_CORE-PadM24) -> VCC_CORE
- JCPU1 pad M26: unconnected-(JCPU1G-VCC_CORE-PadM26) -> VCC_CORE
- JCPU1 pad M28: unconnected-(JCPU1G-VCC_CORE-PadM28) -> VCC_CORE
- JCPU1 pad M30: unconnected-(JCPU1G-VCC_CORE-PadM30) -> VCC_CORE
- JCPU1 pad M32: unconnected-(JCPU1G-VCC_CORE-PadM32) -> VCC_CORE
- JCPU1 pad M33: unconnected-(JCPU1H-VCCGT-PadM33) -> VCC_iGPU
- JCPU1 pad M34: unconnected-(JCPU1H-VCCGT-PadM34) -> VCC_iGPU
- JCPU1 pad M36: unconnected-(JCPU1H-VCCGT-PadM36) -> VCC_iGPU
- JCPU1 pad M38: unconnected-(JCPU1H-VCCGT-PadM38) -> VCC_iGPU
- JCPU1 pad M40: unconnected-(JCPU1H-VCCGT-PadM40) -> VCC_iGPU
- JCPU1 pad M8: unconnected-(JCPU1I-VCCIO-PadM8) -> VCCIO
- JCPU1 pad N34: unconnected-(JCPU1H-VCCGT-PadN34) -> VCC_iGPU
- JCPU1 pad N35: unconnected-(JCPU1H-VCCGT-PadN35) -> VCC_iGPU
- JCPU1 pad N36: unconnected-(JCPU1H-VCCGT-PadN36) -> VCC_iGPU
- JCPU1 pad N37: unconnected-(JCPU1H-VCCGT-PadN37) -> VCC_iGPU
- JCPU1 pad N38: unconnected-(JCPU1H-VCCGT-PadN38) -> VCC_iGPU
- JCPU1 pad N39: unconnected-(JCPU1H-VCCGT-PadN39) -> VCC_iGPU
- JCPU1 pad N40: unconnected-(JCPU1H-VCCGT-PadN40) -> VCC_iGPU
- JCPU1 pad N7: unconnected-(JCPU1I-VCCSA-PadN7) -> VCCSA
- JCPU1 pad P33: unconnected-(JCPU1H-VCCGT-PadP33) -> VCC_iGPU
- JCPU1 pad P34: unconnected-(JCPU1H-VCCGT-PadP34) -> VCC_iGPU
- JCPU1 pad P36: unconnected-(JCPU1H-VCCGT-PadP36) -> VCC_iGPU
- JCPU1 pad P38: unconnected-(JCPU1H-VCCGT-PadP38) -> VCC_iGPU
- JCPU1 pad P40: unconnected-(JCPU1H-VCCGT-PadP40) -> VCC_iGPU
- JCPU1 pad P7: unconnected-(JCPU1I-VCCSA-PadP7) -> VCCSA
- JCPU1 pad P8: unconnected-(JCPU1I-VCCIO-PadP8) -> VCCIO
- JCPU1 pad R34: unconnected-(JCPU1H-VCCGT-PadR34) -> VCC_iGPU
- JCPU1 pad R35: unconnected-(JCPU1H-VCCGT-PadR35) -> VCC_iGPU
- JCPU1 pad R36: unconnected-(JCPU1H-VCCGT-PadR36) -> VCC_iGPU
- JCPU1 pad R37: unconnected-(JCPU1H-VCCGT-PadR37) -> VCC_iGPU
- JCPU1 pad R38: unconnected-(JCPU1H-VCCGT-PadR38) -> VCC_iGPU
- JCPU1 pad R39: unconnected-(JCPU1H-VCCGT-PadR39) -> VCC_iGPU
- JCPU1 pad R40: unconnected-(JCPU1H-VCCGT-PadR40) -> VCC_iGPU
- JCPU1 pad R7: unconnected-(JCPU1I-VCCSA-PadR7) -> VCCSA
- JCPU1 pad T33: unconnected-(JCPU1H-VCCGT-PadT33) -> VCC_iGPU
- JCPU1 pad T34: unconnected-(JCPU1H-VCCGT-PadT34) -> VCC_iGPU
- JCPU1 pad T36: unconnected-(JCPU1H-VCCGT-PadT36) -> VCC_iGPU
- JCPU1 pad T38: unconnected-(JCPU1H-VCCGT-PadT38) -> VCC_iGPU
- JCPU1 pad T40: unconnected-(JCPU1H-VCCGT-PadT40) -> VCC_iGPU
- JCPU1 pad T7: unconnected-(JCPU1I-VCCSA-PadT7) -> VCCSA
- JCPU1 pad T8: unconnected-(JCPU1I-VCCIO-PadT8) -> VCCIO
- JCPU1 pad U1: unconnected-(JCPU1D-PROC_AUDIO_SDO-PadU1) -> CPU_DisplayAudio_SDO
- JCPU1 pad U34: unconnected-(JCPU1H-VCCGT-PadU34) -> VCC_iGPU
- JCPU1 pad U35: unconnected-(JCPU1H-VCCGT-PadU35) -> VCC_iGPU
- JCPU1 pad U36: unconnected-(JCPU1H-VCCGT-PadU36) -> VCC_iGPU
- JCPU1 pad U37: unconnected-(JCPU1H-VCCGT-PadU37) -> VCC_iGPU
- JCPU1 pad U38: unconnected-(JCPU1H-VCCGT-PadU38) -> VCC_iGPU
- JCPU1 pad U39: unconnected-(JCPU1H-VCCGT-PadU39) -> VCC_iGPU
- JCPU1 pad U40: unconnected-(JCPU1H-VCCGT-PadU40) -> VCC_iGPU
- JCPU1 pad U7: unconnected-(JCPU1I-VCCSA-PadU7) -> VCCSA
- JCPU1 pad U8: unconnected-(JCPU1I-VCCIO-PadU8) -> VCCIO
- JCPU1 pad V2: unconnected-(JCPU1D-PROC_AUDIO_SDI-PadV2) -> CPU_DisplayAudio_SDI
- JCPU1 pad V3: unconnected-(JCPU1D-PROC_AUDIO_CLK-PadV3) -> CPU_DisplayAudio_CLK
- JCPU1 pad V33: unconnected-(JCPU1H-VCCGT-PadV33) -> VCC_iGPU
- JCPU1 pad V34: unconnected-(JCPU1H-VCCGT-PadV34) -> VCC_iGPU
- JCPU1 pad V36: unconnected-(JCPU1H-VCCGT-PadV36) -> VCC_iGPU
- JCPU1 pad V38: unconnected-(JCPU1H-VCCGT-PadV38) -> VCC_iGPU
- JCPU1 pad V40: unconnected-(JCPU1H-VCCGT-PadV40) -> VCC_iGPU
- JCPU1 pad V5: unconnected-(JCPU1I-VCCST-PadV5) -> VCCST
- JCPU1 pad V6: unconnected-(JCPU1I-VCCST-PadV6) -> VCCST
- JCPU1 pad V7: unconnected-(JCPU1I-VCCSA-PadV7) -> VCCSA
- JCPU1 pad W34: unconnected-(JCPU1H-VCCGT-PadW34) -> VCC_iGPU
- JCPU1 pad W35: unconnected-(JCPU1H-VCCGT-PadW35) -> VCC_iGPU
- JCPU1 pad W36: unconnected-(JCPU1H-VCCGT-PadW36) -> VCC_iGPU
- JCPU1 pad W37: unconnected-(JCPU1H-VCCGT-PadW37) -> VCC_iGPU
- JCPU1 pad W38: unconnected-(JCPU1H-VCCGT-PadW38) -> VCC_iGPU
- JCPU1 pad W7: unconnected-(JCPU1I-VCCSA-PadW7) -> VCCSA
- JCPU1 pad W8: unconnected-(JCPU1I-VCCIO-PadW8) -> VCCIO
- JCPU1 pad Y33: unconnected-(JCPU1H-VCCGT-PadY33) -> VCC_iGPU
- JCPU1 pad Y34: unconnected-(JCPU1H-VCCGT-PadY34) -> VCC_iGPU
- JCPU1 pad Y36: unconnected-(JCPU1H-VCCGT-PadY36) -> VCC_iGPU
- JCPU1 pad Y38: unconnected-(JCPU1H-VCCGT-PadY38) -> VCC_iGPU
- JCPU1 pad Y6: unconnected-(JCPU1I-VCCSA-PadY6) -> VCCSA
- JCPU1 pad Y7: unconnected-(JCPU1I-VCCSA-PadY7) -> VCCSA
- JCPU1 pad Y8: unconnected-(JCPU1I-VCCSA-PadY8) -> VCCSA
- UPCH1 pad AL13: unconnected-(UPCH1E-GPP_I5/DDPB_CTRLCLK-PadAL13) -> iGPU_DDI1_SCL
- UPCH1 pad AM2: unconnected-(UPCH1D-HDACPU_SDO-PadAM2) -> Net-(UPCH1D-HDACPU_SDO)
- UPCH1 pad AM3: unconnected-(UPCH1D-HDACPU_SCLK-PadAM3) -> Net-(UPCH1D-HDACPU_SCLK)
- UPCH1 pad AN3: unconnected-(UPCH1D-HDACPU_SDI-PadAN3) -> Net-(UPCH1D-HDACPU_SDI)
- UPCH1 pad AR8: unconnected-(UPCH1E-GPP_I6/DDPB_CTRLDATA-PadAR8) -> iGPU_DDI1_SDA
